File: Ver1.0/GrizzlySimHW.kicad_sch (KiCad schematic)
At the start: 244 parts, among them J1 Screw_Terminal_01x02, J10 Screw_Terminal_01x02, J14 GND, J15 GND, J26 GND, J3 Screw_Terminal_01x02, J31 GND, J37 PH2-14-UA, J5 GND, J6 0-10VDC Input, J7 RJ12 - EcoNet, J8 GND, J9 GND, P1 RPi Header, U10 SN74LV1T34DCK, U13 SP3485EN, U14 OPA192IDBVR, U15 OPA192IDBVR, U16 OPA192IDBVR, U17 OPA192IDBVR, U19 MCP4728-E_UN, U2 SN74LV1T34DCK, U20 MCP4728-E_UN, U21 OPA192IDBVR, U22 OPA192IDBVR, U23 OPA192IDBVR, U24 OPA192IDBVR, U25 TPS54560DDAR, U26 AD5245BRJZ100-RL7, U27 AD5245BRJZ100-RL7, U28 OPA192IDBVR, U29 OPA192IDBVR, U30 OPA192IDBVR, U31 OPA192IDBVR, U32 TPS54560DDAR, U33 AD5245BRJZ100-RL7, U34 AD5245BRJZ100-RL7, U35 MCP4728-E_UN, U36 MCP4728-E_UN, U37 OPA192IDBVR, U38 OPA192IDBVR, U39 OPA192IDBVR, U40 OPA192IDBVR, U41 AD5245BRJZ100-RL7, U42 AD5245BRJZ100-RL7, U43 AD5245BRJZ100-RL7, U44 AD5245BRJZ100-RL7, U45 OPA192IDBVR, U46 OPA192IDBVR, U47 OPA192IDBVR, U48 OPA192IDBVR, U49 TCA9548APWR, U5 SN74LV1T34DCK, U50 MCP4728-E_UN, U51 MCP4728-E_UN, U52 AD5245BRJZ100-RL7, U53 AD5245BRJZ100-RL7, U54 OPA192IDBVR, U55 OPA192IDBVR, U56 OPA192IDBVR, U57 OPA192IDBVR, U58 AD5245BRJZ100-RL7, U59 AD5245BRJZ100-RL7, U6 MCP3208, U60 AD5245BRJZ100-RL7, U61 AD5245BRJZ100-RL7, U7 SN74LV1T34DCK

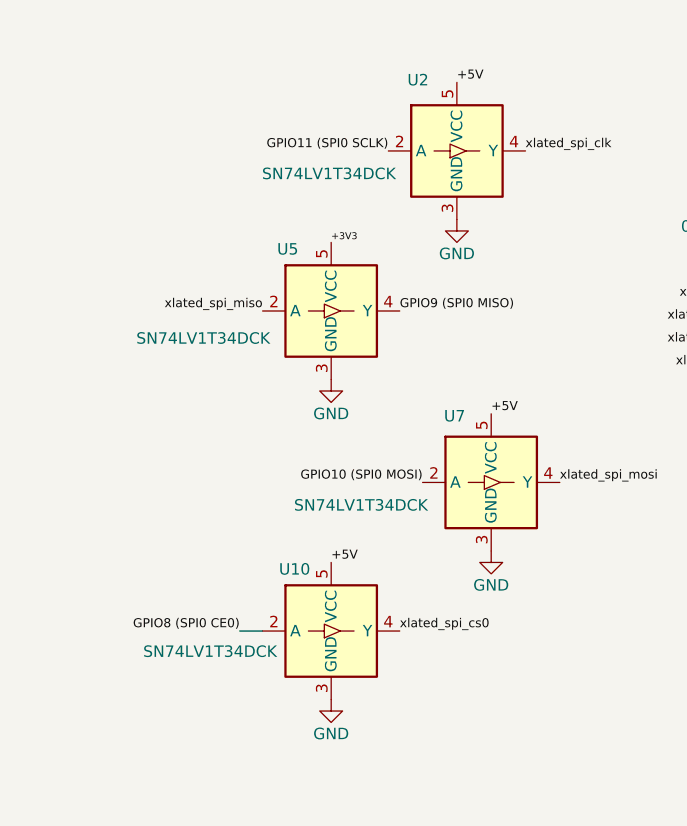
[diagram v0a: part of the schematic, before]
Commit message: Updated Translator Part
Changed the part number and LSCS Part number on the schematic and updated the BOM
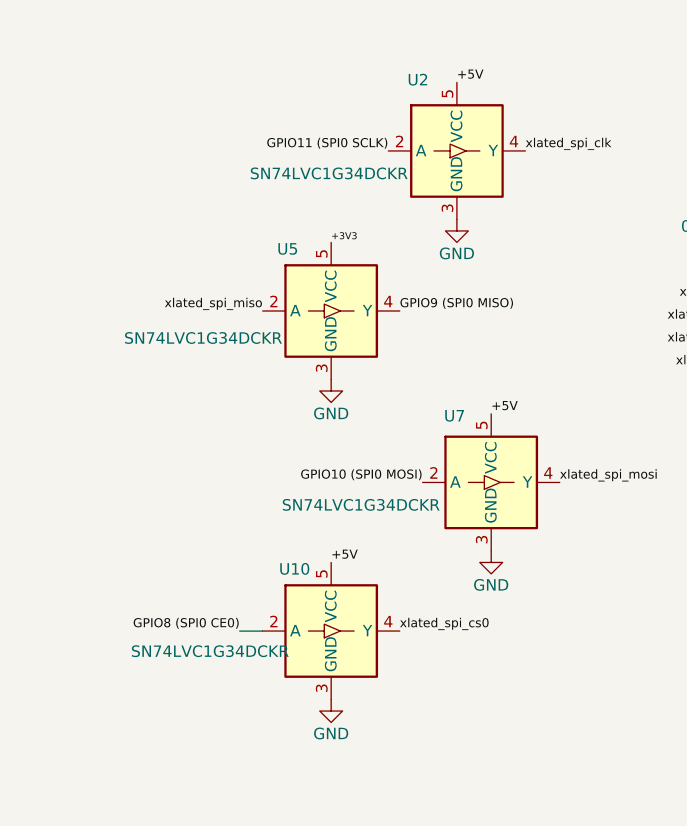
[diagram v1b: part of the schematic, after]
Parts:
- U10, U5, U7: value SN74LV1T34DCK -> SN74LVC1G34DCKR; LCSC Part# C22112 -> C353880
- U2: value SN74LV1T34DCK -> SN74LVC1G34DCKR; LCDC Part# C22112 -> C353880
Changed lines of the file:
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@@
 			)
 		)
-		(property "Value" "SN74LV1T34DCK"
+		(property "Value" "SN74LVC1G34DCKR"
 			(at 33.528 157.226 0)
 			(effects
@@
 			)
 		)
-		(property "LCSC Part#" "C22112"
+		(property "LCSC Part#" "C353880"
 			(at 46.99 154.94 0)
 			(effects
@@
 			)
 		)
-		(property "Value" "SN74LV1T34DCK"
+		(property "Value" "SN74LVC1G34DCKR"
 			(at 32.766 122.428 0)
 			(effects
@@
 			)
 		)
-		(property "LCSC Part#" "C22112"
+		(property "LCSC Part#" "C353880"
 			(at 46.99 119.38 0)
 			(effects
@@
 			)
 		)
-		(property "Value" "SN74LV1T34DCK"
+		(property "Value" "SN74LVC1G34DCKR"
 			(at 50.292 140.97 0)
 			(effects
@@
 			)
 		)
-		(property "LCSC Part#" "C22112"
+		(property "LCSC Part#" "C353880"
 			(at 64.77 138.43 0)
 			(effects
@@
 			)
 		)
-		(property "Value" "SN74LV1T34DCK"
+		(property "Value" "SN74LVC1G34DCKR"
 			(at 46.736 104.14 0)
 			(effects
@@
 			)
 		)
-		(property "LCDC Part#" "C22112"
+		(property "LCDC Part#" "C353880"
 			(at 60.96 101.6 0)
 			(effects
